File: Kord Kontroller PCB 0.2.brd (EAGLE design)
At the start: 242.5 x 100 mm, 190 parts, among them J1 MIDIOUTB, J2 MIDIOUTA, J3 FTSH-105-01-L-DV-KJ, SW2 SPST_TACT-KMR2, U1 AP2112K-3.3, U2 ATSAMD51J19A-AUT, U3 SN74LV4T125PWR, Y1 ECS-.327-12.5-17X-TR

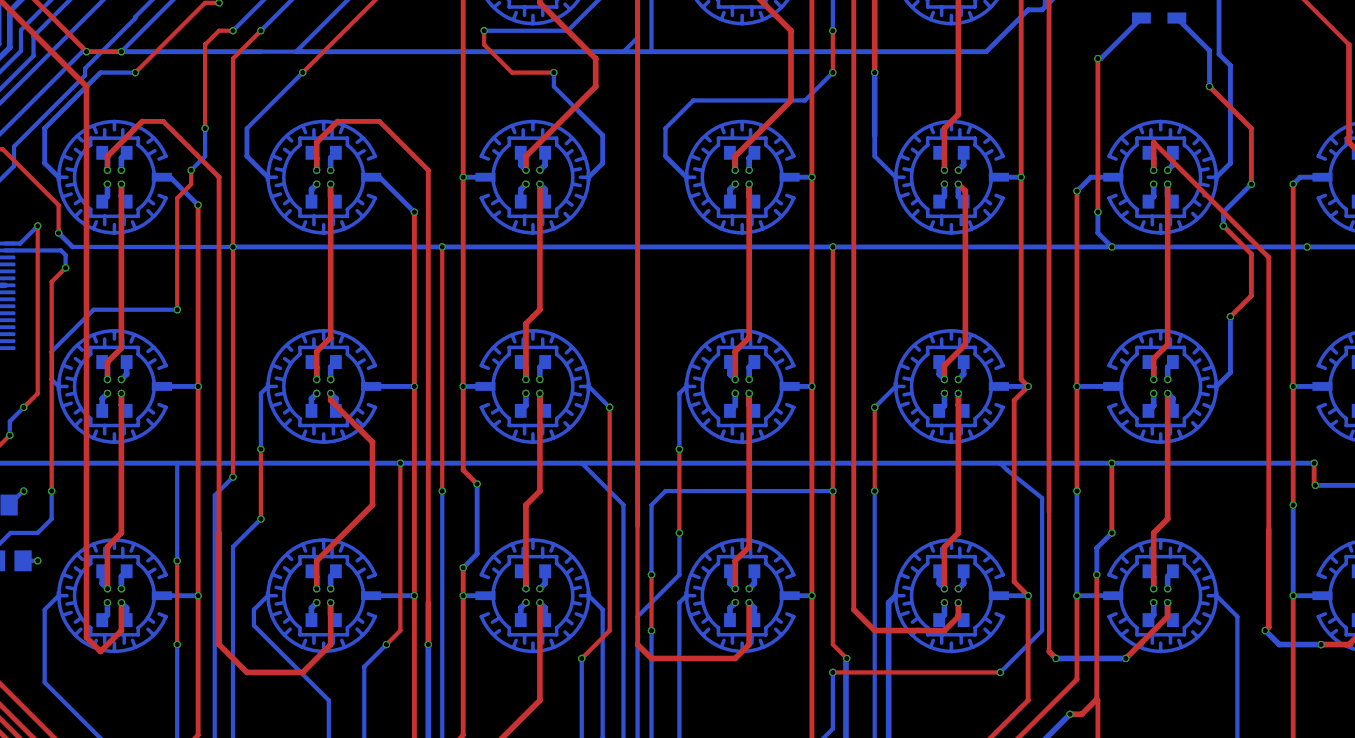
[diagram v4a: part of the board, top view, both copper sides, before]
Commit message: Fixed some right angle traces
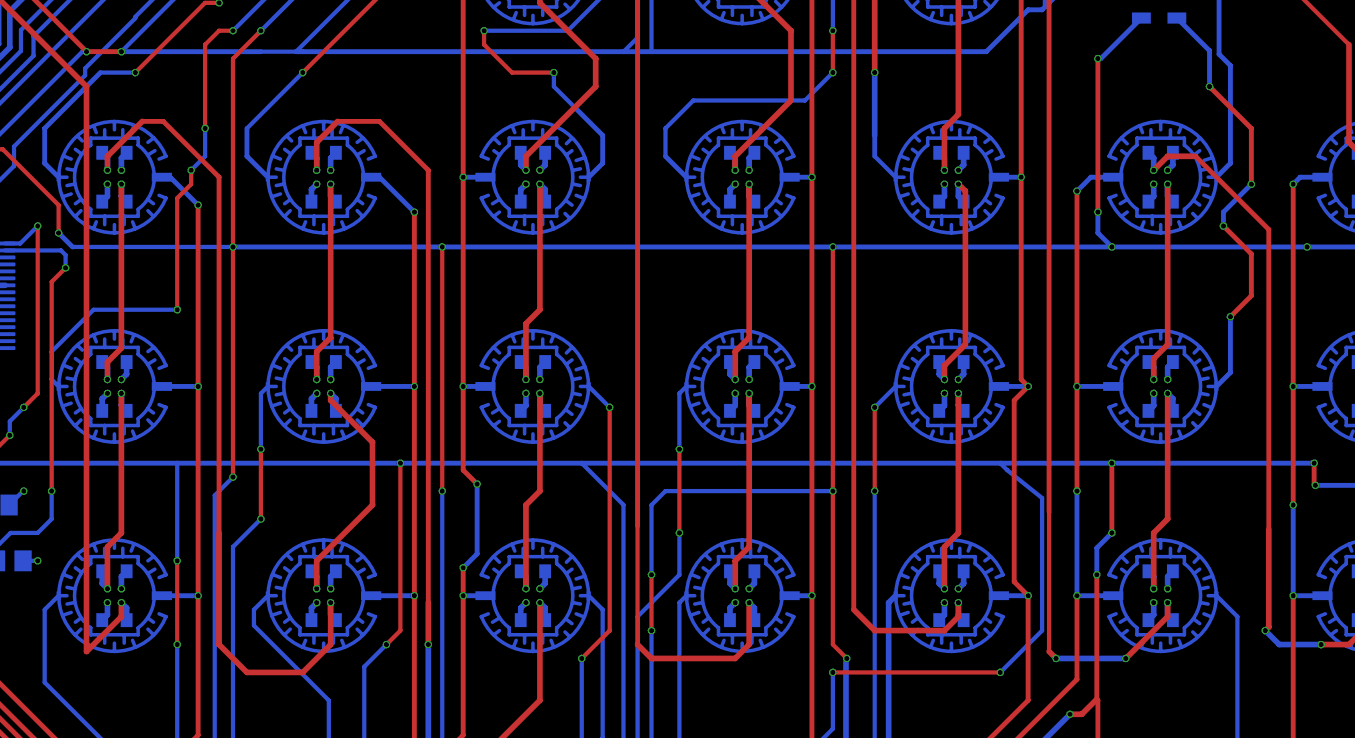
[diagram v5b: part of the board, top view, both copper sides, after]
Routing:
- net N$13: track 53.6 -> 52.7 mm
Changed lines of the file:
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@@
 <contactref element="LED3" pad="3"/>
 <contactref element="LED4" pad="1"/>
-<wire x1="225.25" y1="46.75" x2="225.25" y2="27.25" width="0.35" layer="1"/>
-<wire x1="225.25" y1="46.75" x2="217" y2="55" width="0.35" layer="1"/>
+<wire x1="225.25" y1="48.75" x2="225.25" y2="27.25" width="0.35" layer="1"/>
+<wire x1="225.25" y1="48.75" x2="220" y2="54" width="0.35" layer="1"/>
 <wire x1="233.375" y1="20.75" x2="233" y2="21.125" width="0.4064" layer="16"/>
 <wire x1="233" y1="21.125" x2="233" y2="22" width="0.4064" layer="16"/>
 <via x="233" y="22" extent="1-16" drill="0.35"/>
-<wire x1="217" y1="55" x2="217" y2="53" width="0.4064" layer="1"/>
+<wire x1="220" y1="54" x2="218" y2="54" width="0.4064" layer="1"/>
+<wire x1="218" y1="54" x2="217" y2="53" width="0.4064" layer="1"/>
 <via x="217" y="53" extent="1-16" drill="0.35"/>
 <wire x1="217" y1="53" x2="217" y2="53.875" width="0.4064" layer="16"/>
@@
 <wire x1="126.625" y1="69.25" x2="127" y2="68.875" width="0.4064" layer="16"/>
 <wire x1="127" y1="68.875" x2="127" y2="68" width="0.4064" layer="16"/>
-<wire x1="140.5" y1="19.5" x2="141.5" y2="18.5" width="0.4064" layer="1"/>
-<wire x1="143" y1="20" x2="143" y2="22" width="0.4064" layer="1"/>
-<wire x1="143" y1="20" x2="141.5" y2="18.5" width="0.4064" layer="1"/>
+<wire x1="143" y1="21" x2="143" y2="22" width="0.4064" layer="1"/>
+<wire x1="143" y1="21" x2="140.5" y2="18.5" width="0.4064" layer="1"/>
 <via x="143" y="22" extent="1-16" drill="0.35"/>
 <wire x1="143" y1="22" x2="143.375" y2="21.625" width="0.4064" layer="16"/>
 <wire x1="143.375" y1="21.625" x2="143.375" y2="20.75" width="0.4064" layer="16"/>
-<wire x1="140.5" y1="59" x2="140.5" y2="19.5" width="0.4064" layer="1"/>
+<wire x1="140.5" y1="59" x2="140.5" y2="18.5" width="0.4064" layer="1"/>
 </signal>
 <signal name="N$41">
